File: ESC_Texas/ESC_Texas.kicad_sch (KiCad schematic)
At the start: 69 parts, among them IC1 nRF52840-QFAA-F-R7, IC11 LM3480IM3-3.3_NOPB, IC12 LM3480IM3-3.3_NOPB, J1 Battery-, J12 Conn_01x02, J13 Conn_01x06_Pin, J14 USB_B_Micro, J3 Motor, J4 Battery+, P0.10 TestPoint, P0.11 TestPoint, P0.12 TestPoint, P0.18 TestPoint, P0.7 TestPoint, P0.9 TestPoint, P1.0 TestPoint, P1.9 TestPoint, U1 MCP2515-xSO, U2 TJA1051T, X1 C115962, Y1 CM7V-T1A-32.768kHz, Y2 32MHz

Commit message: 10V input added.
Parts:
- removed J1: Battery-, LIB_2350514-3:SHDRRA3W90P0X350_1X3_1110X920X691P, symbol 2350514-3:2350514-3
- removed J13: Conn_01x06_Pin, Connector_PinHeader_2.54mm:PinHeader_1x06_P2.54mm_Vertical, symbol Connector:Conn_01x06_Pin
- added D14: LED, APTD2012LSURCK:LEDM2012X120N, symbol Device:LED
- added J11: Battery+, LIB_2350514-3:SHDRRA3W90P0X350_1X3_1110X920X691P, symbol 2350514-3:2350514-3
- added J2: RJ45, 87180-066LF:AMPHENOL_87180-066LF, symbol Connector:RJ45
- added R22: ?, Resistor_SMD:R_0805_2012Metric, symbol Device:R
- renumbered Y1 to X1, Y2 to X2, X1 to X3
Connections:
- net +15V: no longer C34.1, IC11.2 (IN)
- net +36V: no longer J4.1
- net GND: now also J4.1, D14.1 (K), J11.3, J2.6
- net P0.08: now also J2.1
- net P0.13: now also J2.2
- net P0.14: now also J2.3
- net P0.17: now also J2.4
- net VDD: now also J2.5
- new net: D14.2 (A), R22.1
- new net +10V: C34.1, IC11.2 (IN), J11.1, R22.2
- no-connect marks 9 -> 10
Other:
- note added: "10 V Input"
- note added: "? mW"
- moved on the sheet: C30, C31, C32, C33, C34, C35, C36, C37, C40, C41, D10, D11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

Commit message: Expanded heat thing
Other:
- moved on the sheet: C30, C31, D11, PS1, R19

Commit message: Added current sensing to 36V net
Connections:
- no-connect marks 10 -> 11
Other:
- added sheet Battery-Current (Battery-Current.kicad_sch)
- note added: "36 V Current measurement"
- moved on the sheet: C30, C31, C33, C34, C40, C41, D11, D12, D13, D14, IC11, IC12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

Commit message: Routing hell
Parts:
- removed J14: USB_B_Micro, Connector_USB:USB_Micro-B_GCT_USB3076-30-A, symbol Connector:USB_B_Micro
- removed J2: RJ45, 87180-066LF:AMPHENOL_87180-066LF, symbol Connector:RJ45
- added J1: RJ45, Connector_RJ:RJ45_Amphenol_54602-x08_Horizontal, symbol Connector:RJ45
- added J2: BD125-10-A-0305-0580-L-B, BD12510A03050580LB, symbol BD125-10-A-0305-0580-L-B:BD125-10-A-0305-0580-L-B
- added JP2: SolderJumper, Jumper:SolderJumper-2_P1.3mm_Open_Pad1.0x1.5mm, symbol Jumper:SolderJumper_2_Open
- added P0.1, P0.2: TestPoint, TestPoint:TestPoint_Pad_D1.0mm, symbol Connector:TestPoint
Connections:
- net GND: now also J1.5, J1.7, J1.8, J2.5
- net P0.02: now also U1.14 (SI)
- net P0.03: now also P0.2.1
- net P0.04: now also P0.1.1
- net P0.05: now also U1.13 (SCK)
- net P0.13: now also J1.2
- net P0.14: now also J1.3
- net P0.17: now also J1.4
- net P0.28: now also U1.15 (SO)
- net P1.08: now also U1.16 (~{CS})
- net P1.15: now also U1.12 (~{INT})
- net SWDCLK: now also J2.4; no longer SWDCLK1.1
- net SWDIO: now also J2.2; no longer SWDIO1.1
- net VDD: now also J1.6, J2.3, J2.8, JP2.1 (A)
- new net: J2.1, JP2.2 (B)
- no-connect marks 11 -> 12
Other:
- moved on the sheet: C1, C10, C11, C12, C13, C14, C2, C3, C30, C31, C32, C33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

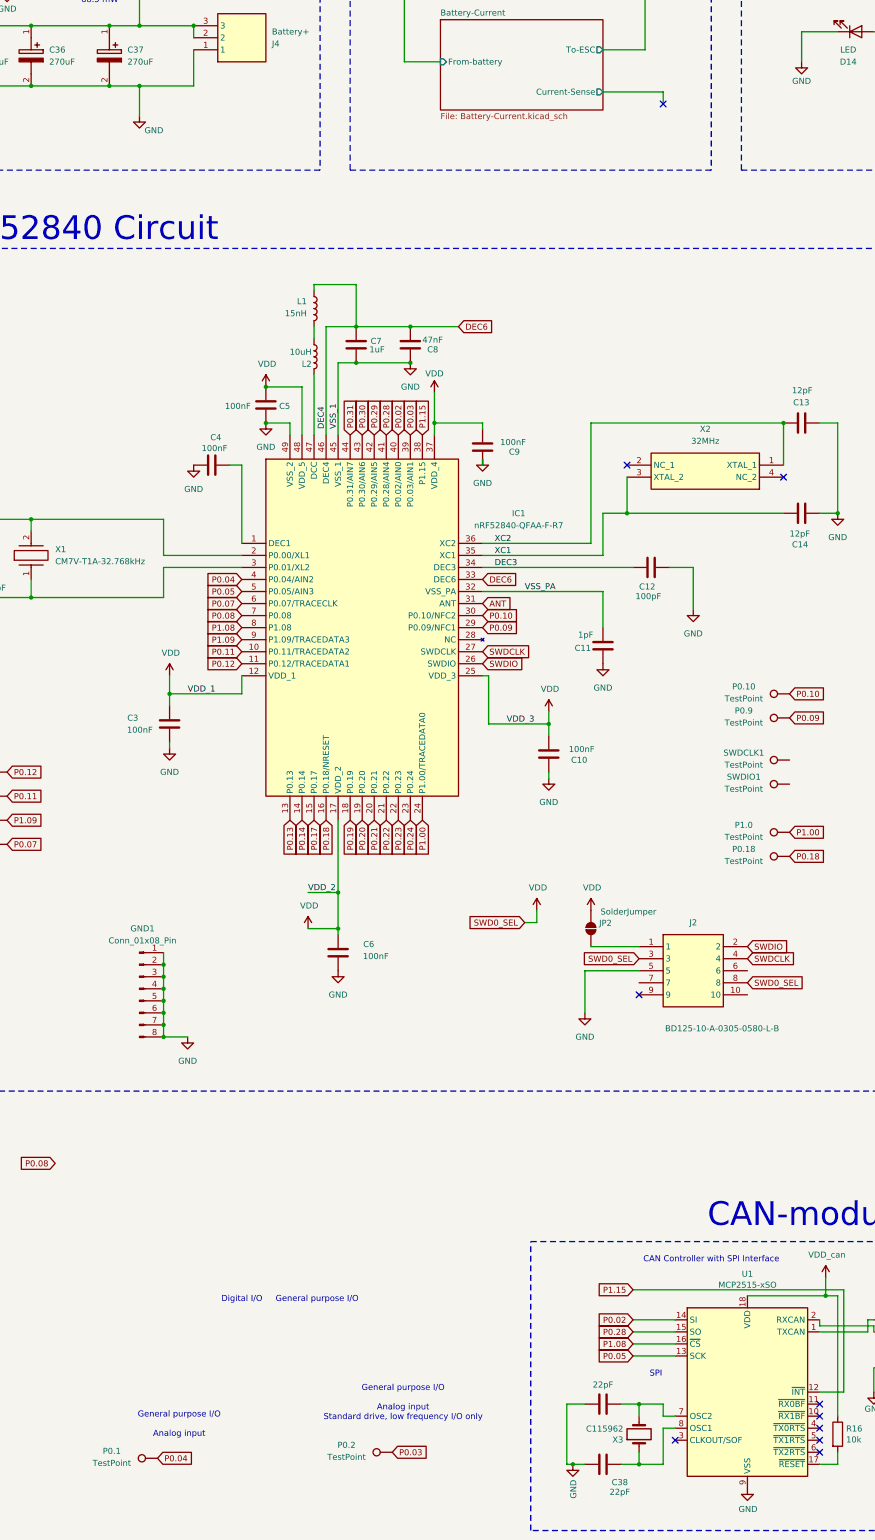
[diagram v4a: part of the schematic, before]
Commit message: Routed pretty much all signals
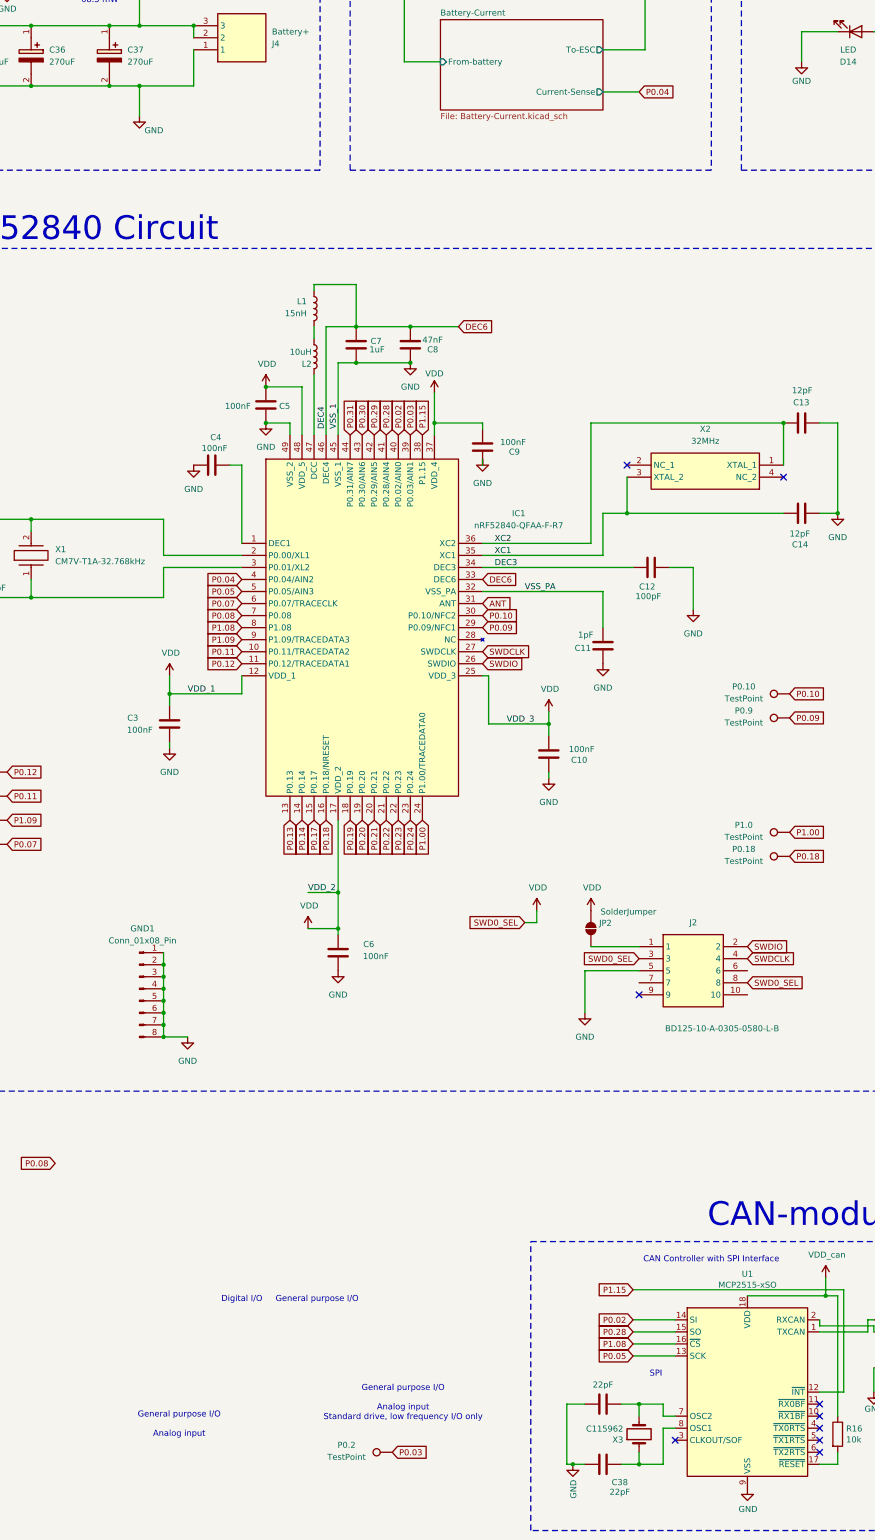
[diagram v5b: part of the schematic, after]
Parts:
- removed P0.1, SWDCLK1, SWDIO1: TestPoint, TestPoint:TestPoint_Pad_D1.0mm, symbol Connector:TestPoint
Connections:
- no-connect marks 12 -> 11
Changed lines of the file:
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@@
 		(at 208.28 353.06)
 	)
-	(no_connect
-		(at 205.74 71.12)
-	)
 	(wire
 		(pts
@@
 	(wire
 		(pts
-			(xy 205.74 68.58) (xy 205.74 71.12)
-		)
-		(stroke
-			(width 0)
-			(type default)
-		)
-	)
-	(wire
-		(pts
 			(xy 322.58 59.69) (xy 322.58 63.5)
 		)
@@
 	(wire
 		(pts
-			(xy 193.04 68.58) (xy 205.74 68.58)
+			(xy 193.04 68.58) (xy 200.66 68.58)
 		)
 		(stroke
@@
 		)
 	)
-	(global_label "P0.04"
-		(shape input)
-		(at 99.06 356.87 0)
-		(fields_autoplaced yes)
-		(effects
-			(font
-				(size 1.27 1.27)
-			)
-			(justify left)
-		)
-		(property "Intersheetrefs" "${INTERSHEET_REFS}"
-			(at 107.5485 356.87 0)
-			(effects
-				(font
-					(size 1.27 1.27)
-				)
-				(justify left)
-				(hide yes)
-			)
-		)
-	)
 	(global_label "P0.08"
 		(shape input)
@@
 		)
 	)
+	(global_label "P0.04"
+		(shape input)
+		(at 200.66 68.58 0)
+		(fields_autoplaced yes)
+		(effects
+			(font
+				(size 1.27 1.27)
+			)
+			(justify left)
+		)
+		(property "Intersheetrefs" "${INTERSHEET_REFS}"
+			(at 209.1485 68.58 0)
+			(effects
+				(font
+					(size 1.27 1.27)
+				)
+				(justify left)
+				(hide yes)
+			)
+		)
+	)
 	(global_label "P0.07"
 		(shape input)
@@
 	)
 	(symbol
-		(lib_id "Connector:TestPoint")
-		(at 232.41 209.55 90)
-		(unit 1)
-		(exclude_from_sim no)
-		(in_bom yes)
-		(on_board yes)
-		(dnp no)
-		(property "Reference" "SWDCLK1"
-			(at 222.758 208.026 90)
-			(effects
-				(font
-					(size 1.27 1.27)
-				)
-			)
-		)
-		(property "Value" "TestPoint"
-			(at 222.758 210.566 90)
-			(effects
-				(font
-					(size 1.27 1.27)
-				)
-			)
-		)
-		(property "Footprint" "TestPoint:TestPoint_Pad_D1.0mm"
-			(at 232.41 204.47 0)
-			(effects
-				(font
-					(size 1.27 1.27)
-				)
-				(hide yes)
-			)
-		)
-		(property "Datasheet" "~"
-			(at 232.41 204.47 0)
-			(effects
-				(font
-					(size 1.27 1.27)
-				)
-				(hide yes)
-			)
-		)
-		(property "Description" "test point"
-			(at 232.41 209.55 0)
-			(effects
-				(font
-					(size 1.27 1.27)
-				)
-				(hide yes)
-			)
-		)
-		(pin "1"
-		)
-		(instances
-			(project "ESC_Texas"
-				(path "/0e3a5351-d2cd-4ecc-a1be-cca9c5f62ea0"
-					(reference "SWDCLK1")
-					(unit 1)
-				)
-			)
-		)
-	)
-	(symbol
 		(lib_id "power:GND")
 		(at 308.61 275.59 0)
@@
 	)
 	(symbol
-		(lib_id "Connector:TestPoint")
-		(at 99.06 356.87 90)
-		(unit 1)
-		(exclude_from_sim no)
-		(in_bom yes)
-		(on_board yes)
-		(dnp no)
-		(property "Reference" "P0.1"
-			(at 89.408 355.346 90)
-			(effects
-				(font
-					(size 1.27 1.27)
-				)
-			)
-		)
-		(property "Value" "TestPoint"
-			(at 89.408 357.886 90)
-			(effects
-				(font
-					(size 1.27 1.27)
-				)
-			)
-		)
-		(property "Footprint" "TestPoint:TestPoint_Pad_D1.0mm"
-			(at 99.06 351.79 0)
-			(effects
-				(font
-					(size 1.27 1.27)
-				)
-				(hide yes)
-			)
-		)
-		(property "Datasheet" "~"
-			(at 99.06 351.79 0)
-			(effects
-				(font
-					(size 1.27 1.27)
-				)
-				(hide yes)
-			)
-		)
-		(property "Description" "test point"
-			(at 99.06 356.87 0)
-			(effects
-				(font
-					(size 1.27 1.27)
-				)
-				(hide yes)
-			)
-		)
-		(pin "1"
-		)
-		(instances
-			(project "ESC_Texas"
-				(path "/0e3a5351-d2cd-4ecc-a1be-cca9c5f62ea0"
-					(reference "P0.1")
-					(unit 1)
-				)
-			)
-		)
-	)
-	(symbol
 		(lib_id "Connector:Screw_Terminal_01x02")
 		(at 298.45 332.74 0)
@@
 					(unit 1)
 				)
-			)
-		)
-	)
-	(symbol
-		(lib_id "Connector:TestPoint")
-		(at 232.41 214.63 90)
-		(unit 1)
-		(exclude_from_sim no)
-		(in_bom yes)
-		(on_board yes)
-		(dnp no)
-		(property "Reference" "SWDIO1"
-			(at 222.758 213.106 90)
-			(effects
-				(font
-					(size 1.27 1.27)
-				)
-			)
-		)
-		(property "Value" "TestPoint"
-			(at 222.758 215.646 90)
-			(effects
-				(font
-					(size 1.27 1.27)
-				)
-			)
-		)
-		(property "Footprint" "TestPoint:TestPoint_Pad_D1.0mm"
-			(at 232.41 209.55 0)
-			(effects
-				(font
-					(size 1.27 1.27)
-				)
-				(hide yes)
-			)
-		)
-		(property "Datasheet" "~"
-			(at 232.41 209.55 0)
-			(effects
-				(font
-					(size 1.27 1.27)
-				)
-				(hide yes)
-			)
-		)
-		(property "Description" "test point"
-			(at 232.41 214.63 0)
-			(effects
-				(font
-					(size 1.27 1.27)
-				)
-				(hide yes)
-			)
-		)
-		(pin "1"
-		)
-		(instances
-			(project "ESC_Texas"
-				(path "/0e3a5351-d2cd-4ecc-a1be-cca9c5f62ea0"
-					(reference "SWDIO1")
-					(unit 1)
-				)

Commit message: Before re routing Hall
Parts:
- removed P0.18: TestPoint, TestPoint:TestPoint_Pad_D1.0mm, symbol Connector:TestPoint
- added P1.1: TestPoint, TestPoint:TestPoint_Pad_D1.0mm, symbol Connector:TestPoint
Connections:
- net P0.18 is gone; now on net nRESET: IC1.16 (P0.18/NRESET)
- net P0.08: now also P1.1.1
- net nRESET: now reaches J2.10
- no-connect marks 11 -> 13
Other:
- moved on the sheet: P1.0

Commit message: Added 5v/3.3v can vdd
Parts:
- removed GND1: Conn_01x08_Pin, Connector_PinHeader_2.54mm:PinHeader_1x08_P2.54mm_Vertical, symbol Connector:Conn_01x08_Pin
- removed P0.2: TestPoint, TestPoint:TestPoint_Pad_D1.0mm, symbol Connector:TestPoint
- added J13: Conn_01x04_Pin, Connector_PinHeader_2.54mm:PinHeader_1x04_P2.54mm_Vertical, symbol Connector:Conn_01x04_Pin
- added J14, J15, J16, J17: Conn_01x01_Pin, Connector_PinHeader_2.54mm:PinHeader_1x01_P2.54mm_Vertical, symbol Connector:Conn_01x01_Pin
- added JP3, JP4: SolderJumper_2_Open, Jumper:SolderJumper-2_P1.3mm_Open_Pad1.0x1.5mm, symbol Jumper:SolderJumper_2_Open
- added SpeedTemp1: TestPoint, TestPoint:TestPoint_Pad_D1.0mm, symbol Connector:TestPoint
- J2: footprint BD12510A03050580LB -> BD125-10-A-0305-0580-L-B:BD12510A03050580LB
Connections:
- net GND: now also J13.1 (Pin_1), J13.2 (Pin_2), J13.3 (Pin_3), J13.4 (Pin_4), J14.1 (Pin_1), J15.1 (Pin_1), J16.1 (Pin_1), J17.1 (Pin_1)
- net VDD: now also R16.1, U1.18 (VDD), JP4.1 (A)
- net VDD_can: now also JP3.2 (B), JP4.2 (B); no longer R16.1, U1.18 (VDD)
- net at J1.1: now also SpeedTemp1.1
- new net +5V: JP3.1 (A)
- no-connect marks 13 -> 12
